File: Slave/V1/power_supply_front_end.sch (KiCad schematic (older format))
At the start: 13 parts, among them U601 AP3015KTR-G1, U602 AP2202K-ADJTRG1

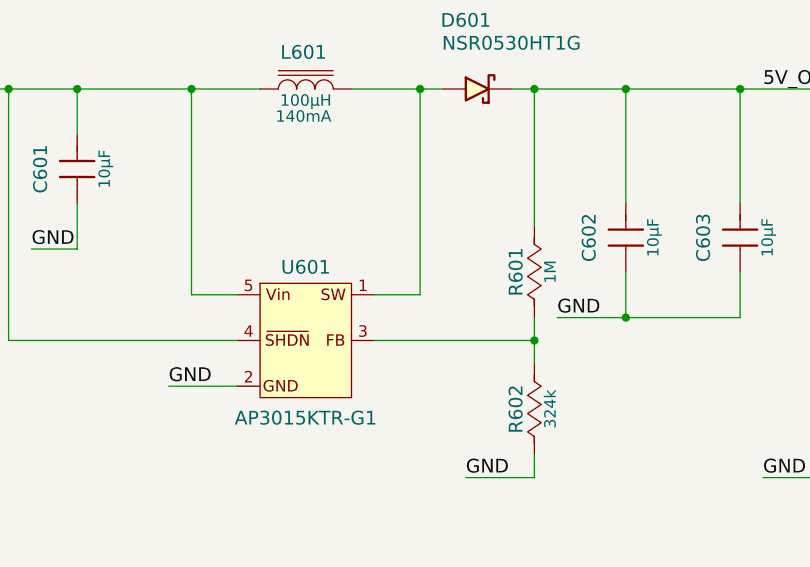
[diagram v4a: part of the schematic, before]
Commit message: placed front end 1 to 5
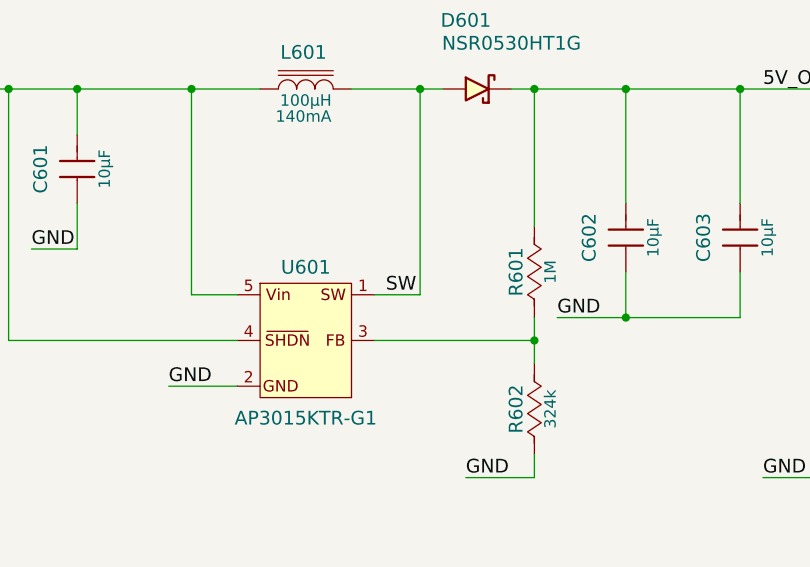
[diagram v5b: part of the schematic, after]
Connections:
- net SW: now reaches D601.2 (Anode), L601.2, U601.1 (SW)
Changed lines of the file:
@@
 $Descr USLetter 11000 8500
 encoding utf-8
-Sheet 14 16
+Sheet 14 36
 Title "Isolated BMS Slave Front End"
 Date ""
@@
 AR Path="/593EFAB4/591CDE38/591B2FEB" Ref="U1401"  Part="1"
 AR Path="/593F9F72/591CDE38/591B2FEB" Ref="U1001"  Part="1"
-AR Path="/593FDFB1/591CDE38/591B2FEB" Ref="U?"  Part="1"
-F 0 "U?" H 4900 3220 60  0000 C CNN
+AR Path="/593FDFB1/591CDE38/591B2FEB" Ref="U1401"  Part="1"
+AR Path="/593FF1B1/591CDE38/591B2FEB" Ref="U1801"  Part="1"
+AR Path="/593FF93E/591CDE38/591B2FEB" Ref="U2201"  Part="1"
+AR Path="/59400152/591CDE38/591B2FEB" Ref="U2601"  Part="1"
+AR Path="/59400D56/591CDE38/591B2FEB" Ref="U3001"  Part="1"
+AR Path="/59400D60/591CDE38/591B2FEB" Ref="U3401"  Part="1"
+F 0 "U601" H 4900 3220 60  0000 C CNN
 F 1 "AP3015KTR-G1" H 4900 2560 60  0000 C CNN
 F 2 "IC:SOT-23-5" H 4900 475 60  0001 C CNN
@@
 AR Path="/593EFAB4/591CDE38/591B30B0" Ref="U1402"  Part="1"
 AR Path="/593F9F72/591CDE38/591B30B0" Ref="U1002"  Part="1"
-AR Path="/593FDFB1/591CDE38/591B30B0" Ref="U?"  Part="1"
-F 0 "U?" H 4500 5300 60  0000 C CNN
+AR Path="/593FDFB1/591CDE38/591B30B0" Ref="U1402"  Part="1"
+AR Path="/593FF1B1/591CDE38/591B30B0" Ref="U1802"  Part="1"
+AR Path="/593FF93E/591CDE38/591B30B0" Ref="U2202"  Part="1"
+AR Path="/59400152/591CDE38/591B30B0" Ref="U2602"  Part="1"
+AR Path="/59400D56/591CDE38/591B30B0" Ref="U3002"  Part="1"
+AR Path="/59400D60/591CDE38/591B30B0" Ref="U3402"  Part="1"
+F 0 "U602" H 4500 5300 60  0000 C CNN
 F 1 "AP2202K-ADJTRG1" H 4500 4660 60  0000 C CNN
 F 2 "IC:SOT-23-5" H 4500 3395 60  0001 C CNN
@@
 AR Path="/593EFAB4/591CDE38/591BCA3D" Ref="C1401"  Part="1"
 AR Path="/593F9F72/591CDE38/591BCA3D" Ref="C1001"  Part="1"
-AR Path="/593FDFB1/591CDE38/591BCA3D" Ref="C?"  Part="1"
-F 0 "C?" H 3850 2260 60  0000 C CNN
+AR Path="/593FDFB1/591CDE38/591BCA3D" Ref="C1401"  Part="1"
+AR Path="/593FF1B1/591CDE38/591BCA3D" Ref="C1801"  Part="1"
+AR Path="/593FF93E/591CDE38/591BCA3D" Ref="C2201"  Part="1"
+AR Path="/59400152/591CDE38/591BCA3D" Ref="C2601"  Part="1"
+AR Path="/59400D56/591CDE38/591BCA3D" Ref="C3001"  Part="1"
+AR Path="/59400D60/591CDE38/591BCA3D" Ref="C3401"  Part="1"
+F 0 "C601" H 3850 2260 60  0000 C CNN
 F 1 "885012107014" H 3850 1750 60  0001 C CNN
 F 2 "Capacitors:C0805" H 3850 1150 60  0001 C CNN
@@
 AR Path="/593EFAB4/591CDE38/591BD4B8" Ref="D1401"  Part="1"
 AR Path="/593F9F72/591CDE38/591BD4B8" Ref="D1001"  Part="1"
-AR Path="/593FDFB1/591CDE38/591BD4B8" Ref="D?"  Part="1"
-F 0 "D?" H 5600 2100 60  0000 C CNN
+AR Path="/593FDFB1/591CDE38/591BD4B8" Ref="D1401"  Part="1"
+AR Path="/593FF1B1/591CDE38/591BD4B8" Ref="D1801"  Part="1"
+AR Path="/593FF93E/591CDE38/591BD4B8" Ref="D2201"  Part="1"
+AR Path="/59400152/591CDE38/591BD4B8" Ref="D2601"  Part="1"
+AR Path="/59400D56/591CDE38/591BD4B8" Ref="D3001"  Part="1"
+AR Path="/59400D60/591CDE38/591BD4B8" Ref="D3401"  Part="1"
+F 0 "D601" H 5600 2100 60  0000 C CNN
 F 1 "NSR0530HT1G" H 5800 2000 60  0000 C CNN
 F 2 "Diodes:SOD-323" H 5680 800 60  0001 C CNN
@@
 AR Path="/593EFAB4/591CDE38/591BE5E6" Ref="C1402"  Part="1"
 AR Path="/593F9F72/591CDE38/591BE5E6" Ref="C1002"  Part="1"
-AR Path="/593FDFB1/591CDE38/591BE5E6" Ref="C?"  Part="1"
-F 0 "C?" H 6250 2560 60  0000 C CNN
+AR Path="/593FDFB1/591CDE38/591BE5E6" Ref="C1402"  Part="1"
+AR Path="/593FF1B1/591CDE38/591BE5E6" Ref="C1802"  Part="1"
+AR Path="/593FF93E/591CDE38/591BE5E6" Ref="C2202"  Part="1"
+AR Path="/59400152/591CDE38/591BE5E6" Ref="C2602"  Part="1"
+AR Path="/59400D56/591CDE38/591BE5E6" Ref="C3002"  Part="1"
+AR Path="/59400D60/591CDE38/591BE5E6" Ref="C3402"  Part="1"
+F 0 "C602" H 6250 2560 60  0000 C CNN
 F 1 "885012107014" H 6250 2050 60  0001 C CNN
 F 2 "Capacitors:C0805" H 6250 1450 60  0001 C CNN
@@
 AR Path="/593EFAB4/591CDE38/591BED58" Ref="C1405"  Part="1"
 AR Path="/593F9F72/591CDE38/591BED58" Ref="C1005"  Part="1"
-AR Path="/593FDFB1/591CDE38/591BED58" Ref="C?"  Part="1"
-F 0 "C?" H 3450 5260 60  0000 C CNN
+AR Path="/593FDFB1/591CDE38/591BED58" Ref="C1405"  Part="1"
+AR Path="/593FF1B1/591CDE38/591BED58" Ref="C1805"  Part="1"
+AR Path="/593FF93E/591CDE38/591BED58" Ref="C2205"  Part="1"
+AR Path="/59400152/591CDE38/591BED58" Ref="C2605"  Part="1"
+AR Path="/59400D56/591CDE38/591BED58" Ref="C3005"  Part="1"
+AR Path="/59400D60/591CDE38/591BED58" Ref="C3405"  Part="1"
+F 0 "C605" H 3450 5260 60  0000 C CNN
 F 1 "885012107014" H 3450 4750 60  0001 C CNN
 F 2 "Capacitors:C0805" H 3450 4150 60  0001 C CNN
@@
 AR Path="/593EFAB4/591CDE38/591BF617" Ref="C1404"  Part="1"
 AR Path="/593F9F72/591CDE38/591BF617" Ref="C1004"  Part="1"
-AR Path="/593FDFB1/591CDE38/591BF617" Ref="C?"  Part="1"
-F 0 "C?" H 6150 5160 60  0000 C CNN
+AR Path="/593FDFB1/591CDE38/591BF617" Ref="C1404"  Part="1"
+AR Path="/593FF1B1/591CDE38/591BF617" Ref="C1804"  Part="1"
+AR Path="/593FF93E/591CDE38/591BF617" Ref="C2204"  Part="1"
+AR Path="/59400152/591CDE38/591BF617" Ref="C2604"  Part="1"
+AR Path="/59400D56/591CDE38/591BF617" Ref="C3004"  Part="1"
+AR Path="/59400D60/591CDE38/591BF617" Ref="C3404"  Part="1"
+F 0 "C604" H 6150 5160 60  0000 C CNN
 F 1 "885012107014" H 6150 4650 60  0001 C CNN
 F 2 "Capacitors:C0805" H 6150 4050 60  0001 C CNN
@@
 AR Path="/593EFAB4/591CDE38/591BFD48" Ref="C1403"  Part="1"
 AR Path="/593F9F72/591CDE38/591BFD48" Ref="C1003"  Part="1"
-AR Path="/593FDFB1/591CDE38/591BFD48" Ref="C?"  Part="1"
-F 0 "C?" H 6750 2560 60  0000 C CNN
+AR Path="/593FDFB1/591CDE38/591BFD48" Ref="C1403"  Part="1"
+AR Path="/593FF1B1/591CDE38/591BFD48" Ref="C1803"  Part="1"
+AR Path="/593FF93E/591CDE38/591BFD48" Ref="C2203"  Part="1"
+AR Path="/59400152/591CDE38/591BFD48" Ref="C2603"  Part="1"
+AR Path="/59400D56/591CDE38/591BFD48" Ref="C3003"  Part="1"
+AR Path="/59400D60/591CDE38/591BFD48" Ref="C3403"  Part="1"
+F 0 "C603" H 6750 2560 60  0000 C CNN
 F 1 "885012107014" H 6750 2050 60  0001 C CNN
 F 2 "Capacitors:C0805" H 6750 1450 60  0001 C CNN
@@
 AR Path="/593EFAB4/591CDE38/591C2F0F" Ref="R1401"  Part="1"
 AR Path="/593F9F72/591CDE38/591C2F0F" Ref="R1001"  Part="1"
-AR Path="/593FDFB1/591CDE38/591C2F0F" Ref="R?"  Part="1"
-F 0 "R?" H 5900 2680 60  0000 C CNN
+AR Path="/593FDFB1/591CDE38/591C2F0F" Ref="R1401"  Part="1"
+AR Path="/593FF1B1/591CDE38/591C2F0F" Ref="R1801"  Part="1"
+AR Path="/593FF93E/591CDE38/591C2F0F" Ref="R2201"  Part="1"
+AR Path="/59400152/591CDE38/591C2F0F" Ref="R2601"  Part="1"
+AR Path="/59400D56/591CDE38/591C2F0F" Ref="R3001"  Part="1"
+AR Path="/59400D60/591CDE38/591C2F0F" Ref="R3401"  Part="1"
+F 0 "R601" H 5900 2680 60  0000 C CNN
 F 1 "RC0805JR-071ML" H 5900 2300 50  0001 C CNN
 F 2 "Resistors:R0805" H 5900 1700 30  0001 C CNN
@@
 AR Path="/593EFAB4/591CDE38/591C3C0D" Ref="R1402"  Part="1"
 AR Path="/593F9F72/591CDE38/591C3C0D" Ref="R1002"  Part="1"
-AR Path="/593FDFB1/591CDE38/591C3C0D" Ref="R?"  Part="1"
-F 0 "R?" H 5900 3280 60  0000 C CNN
+AR Path="/593FDFB1/591CDE38/591C3C0D" Ref="R1402"  Part="1"
+AR Path="/593FF1B1/591CDE38/591C3C0D" Ref="R1802"  Part="1"
+AR Path="/593FF93E/591CDE38/591C3C0D" Ref="R2202"  Part="1"
+AR Path="/59400152/591CDE38/591C3C0D" Ref="R2602"  Part="1"
+AR Path="/59400D56/591CDE38/591C3C0D" Ref="R3002"  Part="1"
+AR Path="/59400D60/591CDE38/591C3C0D" Ref="R3402"  Part="1"
+F 0 "R602" H 5900 3280 60  0000 C CNN
 F 1 "RC0805FR-07324KL" H 5900 2900 50  0001 C CNN
 F 2 "Resistors:R0805" H 5900 2300 30  0001 C CNN
@@
 AR Path="/593EFAB4/591CDE38/5938E158" Ref="R1403"  Part="1"
 AR Path="/593F9F72/591CDE38/5938E158" Ref="R1003"  Part="1"
-AR Path="/593FDFB1/591CDE38/5938E158" Ref="R?"  Part="1"
-F 0 "R?" H 5200 5180 60  0000 C CNN
+AR Path="/593FDFB1/591CDE38/5938E158" Ref="R1403"  Part="1"
+AR Path="/593FF1B1/591CDE38/5938E158" Ref="R1803"  Part="1"
+AR Path="/593FF93E/591CDE38/5938E158" Ref="R2203"  Part="1"
+AR Path="/59400152/591CDE38/5938E158" Ref="R2603"  Part="1"
+AR Path="/59400D56/591CDE38/5938E158" Ref="R3003"  Part="1"
+AR Path="/59400D60/591CDE38/5938E158" Ref="R3403"  Part="1"
+F 0 "R603" H 5200 5180 60  0000 C CNN
 F 1 "RC0805JR-074K7L" H 5200 4800 50  0001 C CNN
 F 2 "Resistors:R0805" H 5200 4200 30  0001 C CNN
@@
 AR Path="/593EFAB4/591CDE38/593DE9E8" Ref="R1404"  Part="1"
 AR Path="/593F9F72/591CDE38/593DE9E8" Ref="R1004"  Part="1"
-AR Path="/593FDFB1/591CDE38/593DE9E8" Ref="R?"  Part="1"
-F 0 "R?" H 5200 5880 60  0000 C CNN
+AR Path="/593FDFB1/591CDE38/593DE9E8" Ref="R1404"  Part="1"
+AR Path="/593FF1B1/591CDE38/593DE9E8" Ref="R1804"  Part="1"
+AR Path="/593FF93E/591CDE38/593DE9E8" Ref="R2204"  Part="1"
+AR Path="/59400152/591CDE38/593DE9E8" Ref="R2604"  Part="1"
+AR Path="/59400D56/591CDE38/593DE9E8" Ref="R3004"  Part="1"
+AR Path="/59400D60/591CDE38/593DE9E8" Ref="R3404"  Part="1"
+F 0 "R604" H 5200 5880 60  0000 C CNN
 F 1 "RC0805FR-0712K1L" H 5200 5500 50  0001 C CNN
 F 2 "Resistors:R0805" H 5200 4900 30  0001 C CNN
@@
 AR Path="/593EFAB4/591CDE38/593D0CFC" Ref="L1401"  Part="1"
 AR Path="/593F9F72/591CDE38/593D0CFC" Ref="L1001"  Part="1"
-AR Path="/593FDFB1/591CDE38/593D0CFC" Ref="L?"  Part="1"
-F 0 "L?" H 4890 1960 60  0000 C CNN
+AR Path="/593FDFB1/591CDE38/593D0CFC" Ref="L1401"  Part="1"
+AR Path="/593FF1B1/591CDE38/593D0CFC" Ref="L1801"  Part="1"
+AR Path="/593FF93E/591CDE38/593D0CFC" Ref="L2201"  Part="1"
+AR Path="/59400152/591CDE38/593D0CFC" Ref="L2601"  Part="1"
+AR Path="/59400D56/591CDE38/593D0CFC" Ref="L3001"  Part="1"
+AR Path="/59400D60/591CDE38/593D0CFC" Ref="L3401"  Part="1"
+F 0 "L601" H 4890 1960 60  0000 C CNN
 F 1 "MLZ2012N101LT000" H 4900 1500 60  0001 C CNN
 F 2 "Inductors:I0805" H 4900 900 60  0001 C CNN
@@
 Text Label 3700 2500 0    60   ~ 0
 GND
+Text Label 5250 2700 0    60   ~ 0
+SW
 $EndSCHEMATC

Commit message: front end done
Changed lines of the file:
@@
 AR Path="/59400D56/591CDE38/591B2FEB" Ref="U3001"  Part="1"
 AR Path="/59400D60/591CDE38/591B2FEB" Ref="U3401"  Part="1"
-F 0 "U601" H 4900 3220 60  0000 C CNN
+F 0 "U3401" H 4900 3220 60  0000 C CNN
 F 1 "AP3015KTR-G1" H 4900 2560 60  0000 C CNN
 F 2 "IC:SOT-23-5" H 4900 475 60  0001 C CNN
@@
 AR Path="/59400D56/591CDE38/591B30B0" Ref="U3002"  Part="1"
 AR Path="/59400D60/591CDE38/591B30B0" Ref="U3402"  Part="1"
-F 0 "U602" H 4500 5300 60  0000 C CNN
+F 0 "U3402" H 4500 5300 60  0000 C CNN
 F 1 "AP2202K-ADJTRG1" H 4500 4660 60  0000 C CNN
 F 2 "IC:SOT-23-5" H 4500 3395 60  0001 C CNN
@@
 AR Path="/59400D56/591CDE38/591BCA3D" Ref="C3001"  Part="1"
 AR Path="/59400D60/591CDE38/591BCA3D" Ref="C3401"  Part="1"
-F 0 "C601" H 3850 2260 60  0000 C CNN
+F 0 "C3401" H 3850 2260 60  0000 C CNN
 F 1 "885012107014" H 3850 1750 60  0001 C CNN
 F 2 "Capacitors:C0805" H 3850 1150 60  0001 C CNN
@@
 AR Path="/59400D56/591CDE38/591BD4B8" Ref="D3001"  Part="1"
 AR Path="/59400D60/591CDE38/591BD4B8" Ref="D3401"  Part="1"
-F 0 "D601" H 5600 2100 60  0000 C CNN
+F 0 "D3401" H 5600 2100 60  0000 C CNN
 F 1 "NSR0530HT1G" H 5800 2000 60  0000 C CNN
 F 2 "Diodes:SOD-323" H 5680 800 60  0001 C CNN
@@
 AR Path="/59400D56/591CDE38/591BE5E6" Ref="C3002"  Part="1"
 AR Path="/59400D60/591CDE38/591BE5E6" Ref="C3402"  Part="1"
-F 0 "C602" H 6250 2560 60  0000 C CNN
+F 0 "C3402" H 6250 2560 60  0000 C CNN
 F 1 "885012107014" H 6250 2050 60  0001 C CNN
 F 2 "Capacitors:C0805" H 6250 1450 60  0001 C CNN
@@
 AR Path="/59400D56/591CDE38/591BED58" Ref="C3005"  Part="1"
 AR Path="/59400D60/591CDE38/591BED58" Ref="C3405"  Part="1"
-F 0 "C605" H 3450 5260 60  0000 C CNN
+F 0 "C3405" H 3450 5260 60  0000 C CNN
 F 1 "885012107014" H 3450 4750 60  0001 C CNN
 F 2 "Capacitors:C0805" H 3450 4150 60  0001 C CNN
@@
 AR Path="/59400D56/591CDE38/591BF617" Ref="C3004"  Part="1"
 AR Path="/59400D60/591CDE38/591BF617" Ref="C3404"  Part="1"
-F 0 "C604" H 6150 5160 60  0000 C CNN
+F 0 "C3404" H 6150 5160 60  0000 C CNN
 F 1 "885012107014" H 6150 4650 60  0001 C CNN
 F 2 "Capacitors:C0805" H 6150 4050 60  0001 C CNN
@@
 AR Path="/59400D56/591CDE38/591BFD48" Ref="C3003"  Part="1"
 AR Path="/59400D60/591CDE38/591BFD48" Ref="C3403"  Part="1"
-F 0 "C603" H 6750 2560 60  0000 C CNN
+F 0 "C3403" H 6750 2560 60  0000 C CNN
 F 1 "885012107014" H 6750 2050 60  0001 C CNN
 F 2 "Capacitors:C0805" H 6750 1450 60  0001 C CNN
@@
 AR Path="/59400D56/591CDE38/591C2F0F" Ref="R3001"  Part="1"
 AR Path="/59400D60/591CDE38/591C2F0F" Ref="R3401"  Part="1"
-F 0 "R601" H 5900 2680 60  0000 C CNN
+F 0 "R3401" H 5900 2680 60  0000 C CNN
 F 1 "RC0805JR-071ML" H 5900 2300 50  0001 C CNN
 F 2 "Resistors:R0805" H 5900 1700 30  0001 C CNN
@@
 AR Path="/59400D56/591CDE38/591C3C0D" Ref="R3002"  Part="1"
 AR Path="/59400D60/591CDE38/591C3C0D" Ref="R3402"  Part="1"
-F 0 "R602" H 5900 3280 60  0000 C CNN
+F 0 "R3402" H 5900 3280 60  0000 C CNN
 F 1 "RC0805FR-07324KL" H 5900 2900 50  0001 C CNN
 F 2 "Resistors:R0805" H 5900 2300 30  0001 C CNN
@@
 AR Path="/59400D56/591CDE38/5938E158" Ref="R3003"  Part="1"
 AR Path="/59400D60/591CDE38/5938E158" Ref="R3403"  Part="1"
-F 0 "R603" H 5200 5180 60  0000 C CNN
+F 0 "R3403" H 5200 5180 60  0000 C CNN
 F 1 "RC0805JR-074K7L" H 5200 4800 50  0001 C CNN
 F 2 "Resistors:R0805" H 5200 4200 30  0001 C CNN
@@
 AR Path="/59400D56/591CDE38/593DE9E8" Ref="R3004"  Part="1"
 AR Path="/59400D60/591CDE38/593DE9E8" Ref="R3404"  Part="1"
-F 0 "R604" H 5200 5880 60  0000 C CNN
+F 0 "R3404" H 5200 5880 60  0000 C CNN
 F 1 "RC0805FR-0712K1L" H 5200 5500 50  0001 C CNN
 F 2 "Resistors:R0805" H 5200 4900 30  0001 C CNN
@@
 AR Path="/59400D56/591CDE38/593D0CFC" Ref="L3001"  Part="1"
 AR Path="/59400D60/591CDE38/593D0CFC" Ref="L3401"  Part="1"
-F 0 "L601" H 4890 1960 60  0000 C CNN
+F 0 "L3401" H 4890 1960 60  0000 C CNN
 F 1 "MLZ2012N101LT000" H 4900 1500 60  0001 C CNN
 F 2 "Inductors:I0805" H 4900 900 60  0001 C CNN

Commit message: Routing signals
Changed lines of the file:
@@
 AR Path="/59400D56/591CDE38/591B2FEB" Ref="U3001"  Part="1"
 AR Path="/59400D60/591CDE38/591B2FEB" Ref="U3401"  Part="1"
-F 0 "U3401" H 4900 3220 60  0000 C CNN
+F 0 "U601" H 4900 3220 60  0000 C CNN
 F 1 "AP3015KTR-G1" H 4900 2560 60  0000 C CNN
 F 2 "IC:SOT-23-5" H 4900 475 60  0001 C CNN
@@
 AR Path="/59400D56/591CDE38/591B30B0" Ref="U3002"  Part="1"
 AR Path="/59400D60/591CDE38/591B30B0" Ref="U3402"  Part="1"
-F 0 "U3402" H 4500 5300 60  0000 C CNN
+F 0 "U602" H 4500 5300 60  0000 C CNN
 F 1 "AP2202K-ADJTRG1" H 4500 4660 60  0000 C CNN
 F 2 "IC:SOT-23-5" H 4500 3395 60  0001 C CNN
@@
 AR Path="/59400D56/591CDE38/591BCA3D" Ref="C3001"  Part="1"
 AR Path="/59400D60/591CDE38/591BCA3D" Ref="C3401"  Part="1"
-F 0 "C3401" H 3850 2260 60  0000 C CNN
+F 0 "C601" H 3850 2260 60  0000 C CNN
 F 1 "885012107014" H 3850 1750 60  0001 C CNN
 F 2 "Capacitors:C0805" H 3850 1150 60  0001 C CNN
@@
 AR Path="/59400D56/591CDE38/591BD4B8" Ref="D3001"  Part="1"
 AR Path="/59400D60/591CDE38/591BD4B8" Ref="D3401"  Part="1"
-F 0 "D3401" H 5600 2100 60  0000 C CNN
+F 0 "D601" H 5600 2100 60  0000 C CNN
 F 1 "NSR0530HT1G" H 5800 2000 60  0000 C CNN
 F 2 "Diodes:SOD-323" H 5680 800 60  0001 C CNN
@@
 AR Path="/59400D56/591CDE38/591BE5E6" Ref="C3002"  Part="1"
 AR Path="/59400D60/591CDE38/591BE5E6" Ref="C3402"  Part="1"
-F 0 "C3402" H 6250 2560 60  0000 C CNN
+F 0 "C602" H 6250 2560 60  0000 C CNN
 F 1 "885012107014" H 6250 2050 60  0001 C CNN
 F 2 "Capacitors:C0805" H 6250 1450 60  0001 C CNN
@@
 AR Path="/59400D56/591CDE38/591BED58" Ref="C3005"  Part="1"
 AR Path="/59400D60/591CDE38/591BED58" Ref="C3405"  Part="1"
-F 0 "C3405" H 3450 5260 60  0000 C CNN
+F 0 "C605" H 3450 5260 60  0000 C CNN
 F 1 "885012107014" H 3450 4750 60  0001 C CNN
 F 2 "Capacitors:C0805" H 3450 4150 60  0001 C CNN
@@
 AR Path="/59400D56/591CDE38/591BF617" Ref="C3004"  Part="1"
 AR Path="/59400D60/591CDE38/591BF617" Ref="C3404"  Part="1"
-F 0 "C3404" H 6150 5160 60  0000 C CNN
+F 0 "C604" H 6150 5160 60  0000 C CNN
 F 1 "885012107014" H 6150 4650 60  0001 C CNN
 F 2 "Capacitors:C0805" H 6150 4050 60  0001 C CNN
@@
 AR Path="/59400D56/591CDE38/591BFD48" Ref="C3003"  Part="1"
 AR Path="/59400D60/591CDE38/591BFD48" Ref="C3403"  Part="1"
-F 0 "C3403" H 6750 2560 60  0000 C CNN
+F 0 "C603" H 6750 2560 60  0000 C CNN
 F 1 "885012107014" H 6750 2050 60  0001 C CNN
 F 2 "Capacitors:C0805" H 6750 1450 60  0001 C CNN
@@
 AR Path="/59400D56/591CDE38/591C2F0F" Ref="R3001"  Part="1"
 AR Path="/59400D60/591CDE38/591C2F0F" Ref="R3401"  Part="1"
-F 0 "R3401" H 5900 2680 60  0000 C CNN
+F 0 "R601" H 5900 2680 60  0000 C CNN
 F 1 "RC0805JR-071ML" H 5900 2300 50  0001 C CNN
 F 2 "Resistors:R0805" H 5900 1700 30  0001 C CNN
@@
 AR Path="/59400D56/591CDE38/591C3C0D" Ref="R3002"  Part="1"
 AR Path="/59400D60/591CDE38/591C3C0D" Ref="R3402"  Part="1"
-F 0 "R3402" H 5900 3280 60  0000 C CNN
+F 0 "R602" H 5900 3280 60  0000 C CNN
 F 1 "RC0805FR-07324KL" H 5900 2900 50  0001 C CNN
 F 2 "Resistors:R0805" H 5900 2300 30  0001 C CNN
@@
 AR Path="/59400D56/591CDE38/5938E158" Ref="R3003"  Part="1"
 AR Path="/59400D60/591CDE38/5938E158" Ref="R3403"  Part="1"
-F 0 "R3403" H 5200 5180 60  0000 C CNN
+F 0 "R603" H 5200 5180 60  0000 C CNN
 F 1 "RC0805JR-074K7L" H 5200 4800 50  0001 C CNN
 F 2 "Resistors:R0805" H 5200 4200 30  0001 C CNN
@@
 AR Path="/59400D56/591CDE38/593DE9E8" Ref="R3004"  Part="1"
 AR Path="/59400D60/591CDE38/593DE9E8" Ref="R3404"  Part="1"
-F 0 "R3404" H 5200 5880 60  0000 C CNN
+F 0 "R604" H 5200 5880 60  0000 C CNN
 F 1 "RC0805FR-0712K1L" H 5200 5500 50  0001 C CNN
 F 2 "Resistors:R0805" H 5200 4900 30  0001 C CNN
@@
 AR Path="/59400D56/591CDE38/593D0CFC" Ref="L3001"  Part="1"
 AR Path="/59400D60/591CDE38/593D0CFC" Ref="L3401"  Part="1"
-F 0 "L3401" H 4890 1960 60  0000 C CNN
+F 0 "L601" H 4890 1960 60  0000 C CNN
 F 1 "MLZ2012N101LT000" H 4900 1500 60  0001 C CNN
 F 2 "Inductors:I0805" H 4900 900 60  0001 C CNN

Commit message: minor
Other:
- note removed: "Changer\npour\n12.1k"
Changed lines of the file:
@@
 $Descr USLetter 11000 8500
 encoding utf-8
-Sheet 14 36
+Sheet 6 36
 Title "Isolated BMS Slave Front End"
 Date ""
@@
 Text HLabel 3400 1800 0    60   Input ~ 0
 Vin
-Text Notes 4700 6000 0    60   ~ 0
-Changer\npour\n12.1k
 Wire Wire Line
 	4600 2900 3600 2900
